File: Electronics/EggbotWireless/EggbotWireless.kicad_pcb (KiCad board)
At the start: 2 copper layers, 115 x 40 mm, 59 parts, among them J1 BATT, J2 Conn_01x04_Female, J3 USB_B_Micro, J4 AVR-ISP-6, J5 Conn_01x03_Female, M1 Stepper_Motor_bipolar, M2 Stepper_Motor_bipolar, M3 Motor_Servo, Q1 FDD8447L, Q2 2N7002, SW1 SW_SPDT, U1 TPS62203DBV, U2 ATmega32A-AU, U3 DW01, U4 FS8205A, U5 CP2102-GMR, U6 LTC4054ES5-4.2, U7 ESP-12E, U8 LM3478, Y1 16MHz

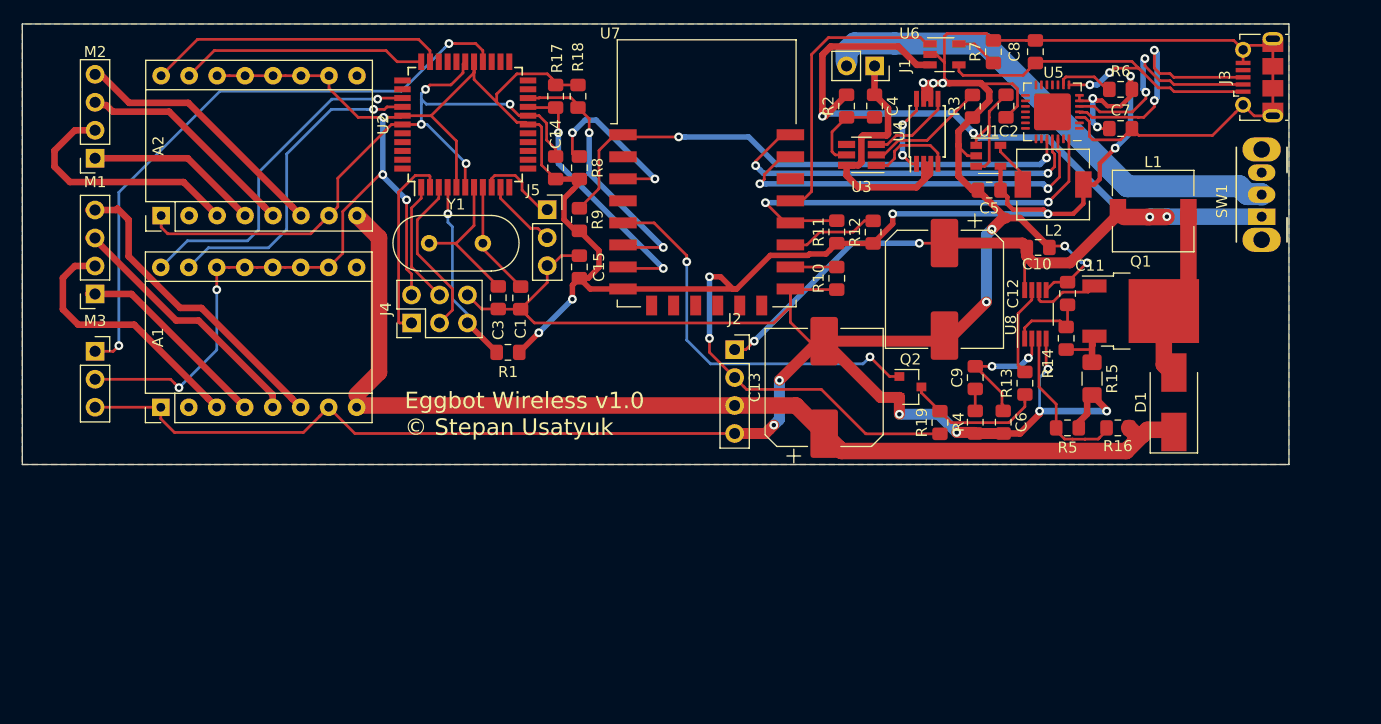
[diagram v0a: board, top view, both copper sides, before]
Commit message: use ft232rl for usb ic, better power handling
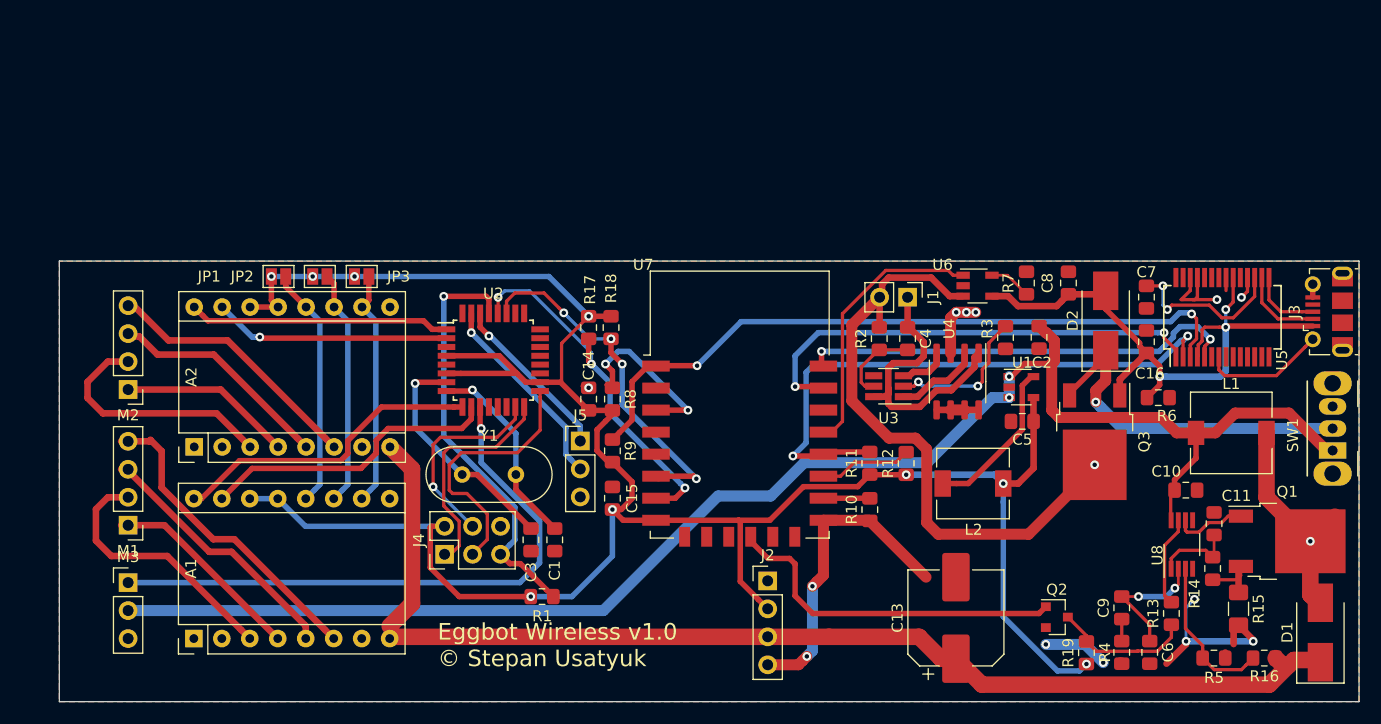
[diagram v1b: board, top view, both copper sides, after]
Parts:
- removed C12: 220uF, Capacitor_SMD:CP_Elec_10x10.5
- added C16: 100nf, Capacitor_SMD:C_0805_2012Metric_Pad1.15x1.40mm_HandSolder, F.Cu at (118.1, 44.9)
- added D2: SK84, Diode_SMD:D_SMB_Handsoldering, F.Cu at (114.4, 42.9)
- added JP1: , Jumper:SolderJumper-2_P1.3mm_Open_Pad1.0x1.5mm, F.Cu at (39.3, 38.9)
- added JP2: , Jumper:SolderJumper-2_P1.3mm_Open_Pad1.0x1.5mm, F.Cu at (43.0, 38.9)
- added JP3: , Jumper:SolderJumper-2_P1.3mm_Open_Pad1.0x1.5mm, F.Cu at (46.8, 38.9)
- added Q3: AOD403, Package_TO_SOT_SMD:TO-252-2, F.Cu at (113.4, 53.9)
- C13: footprint Capacitor_SMD:CP_Elec_10x10.5 -> Capacitor_SMD:CP_Elec_8x10.5
- J1: footprint Connector_PinSocket_2.54mm:PinSocket_1x02_P2.54mm_Vertical -> Connector_PinHeader_2.54mm:PinHeader_1x02_P2.54mm_Vertical
- J2: footprint Connector_PinSocket_2.54mm:PinSocket_1x04_P2.54mm_Vertical -> Connector_PinHeader_2.54mm:PinHeader_1x04_P2.54mm_Vertical
- J5, M3: footprint Connector_PinSocket_2.54mm:PinSocket_1x03_P2.54mm_Vertical -> Connector_PinHeader_2.54mm:PinHeader_1x03_P2.54mm_Vertical
- M1, M2: value Stepper_Motor_bipolar -> (none); footprint Connector_PinSocket_2.54mm:PinSocket_1x04_P2.54mm_Vertical -> Connector_PinHeader_2.54mm:PinHeader_1x04_P2.54mm_Vertical
- R7: value 1K6 -> 2.2K
- SW1: value SW_SPDT -> (none)
- U2: value ATmega32A-AU -> ATmega328P-AU; footprint Package_QFP:TQFP-44_10x10mm_P0.8mm -> Package_QFP:TQFP-32_7x7mm_P0.8mm
- U4: value FS8205A -> DMG4800LSD; footprint Package_SO:TSSOP-8_4.4x3mm_P0.65mm -> Package_SO:SO-8_3.9x4.9mm_P1.27mm
- U5: value CP2102-GMR -> FT232RL; footprint Package_DFN_QFN:QFN-28-1EP_5x5mm_P0.5mm_EP3.35x3.35mm -> Package_SO:SSOP-28_5.3x10.2mm_P0.65mm
- moved R6 28.2 mm to (119.1, 49.9), turned to 180 degrees
- moved L2 28.1 mm to (102.3, 57.7)
- moved C10 25.8 mm to (121.6, 58.3)
- moved D1 24.8 mm to (133.9, 71.2)
- moved R13 24.8 mm to (120.3, 69.5)
- moved C6 24.8 mm to (118.4, 73.1)
- moved Q1 24.8 mm to (130.8, 63.0)
- moved R15 24.8 mm to (126.4, 69.1)
- moved R4 24.8 mm to (115.8, 73.1)
- moved U8 24.8 mm to (121.3, 63.3)
- moved R19 24.8 mm to (112.6, 73.1)
- moved C11 24.8 mm to (124.2, 61.4)
- moved C9 24.8 mm to (115.8, 69.0)
- moved R14 24.8 mm to (124.1, 65.4)
- moved R5 24.8 mm to (124.2, 73.6)
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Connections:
- A1 pad 10: +3V3 -> Net-(A1-Pad10)
- A1 pad 11: +3V3 -> Net-(A1-Pad11)
- A1 pad 12: +3V3 -> Net-(A1-Pad12)
- A1 pad 15: Net-(A1-Pad15) -> STEP1
- A1 pad 16: Net-(A1-Pad16) -> DIR1
- A1 pad 2: Net-(A1-Pad2) -> (no net)
- A1 pad 9: Net-(A1-Pad9) -> (no net)
- A2 pad 10: +3V3 -> Net-(A1-Pad10)
- A2 pad 11: +3V3 -> Net-(A1-Pad11)
- A2 pad 12: +3V3 -> Net-(A1-Pad12)
- A2 pad 15: Net-(A2-Pad15) -> STEP2
- A2 pad 16: Net-(A2-Pad16) -> DIR2
- A2 pad 2: Net-(A2-Pad2) -> (no net)
- A2 pad 9: Net-(A2-Pad9) -> (no net)
- C10 pad 1: +BATT -> +5V
- C2 pad 1: +BATT -> +5V
- C7 pad 1: +3V3 -> GND
- C7 pad 2: GND -> Net-(C7-Pad2)
- J2 pad 1: +BATT -> (no net)
- J3 pad 2: Net-(J3-Pad2) -> USBD-
- J3 pad 3: Net-(J3-Pad3) -> USBD+
- J3 pad 4: Net-(J3-Pad4) -> (no net)
- L1 pad 1: +BATT -> +5V
- M3 pad 2: +3V3 -> +5V
- R1 pad 1: Net-(J4-Pad5) -> +3V3
- R1 pad 2: +3V3 -> Net-(J4-Pad5)
- R2 pad 2: +BATT -> Net-(J1-Pad2)
- R6 pad 1: Net-(R6-Pad1) -> GND
- R6 pad 2: +3V3 -> VBUS
- SW1 pad 1: +BATT -> +5V
- SW1 pad 2: Net-(J1-Pad2) -> Net-(D2-Pad1)
- SW1 pad 3: Net-(SW1-Pad3) -> (no net)
- U1 pad 1: +BATT -> +5V
- U1 pad 3: +BATT -> +5V
- U2 pad 1: Net-(J4-Pad4) -> DIR2
- U2 pad 10: Net-(J5-Pad2) -> STEP1
- U2 pad 11: Net-(U2-Pad11) -> Net-(M3-Pad1)
- U2 pad 12: Net-(U2-Pad12) -> (no net)
- U2 pad 13: Net-(U2-Pad13) -> (no net)
- U2 pad 14: Net-(U2-Pad14) -> (no net)
- U2 pad 15: Net-(U2-Pad15) -> Net-(J4-Pad4)
- U2 pad 16: Net-(U2-Pad16) -> Net-(J4-Pad1)
- U2 pad 17: +3V3 -> Net-(J4-Pad3)
- U2 pad 18: GND -> +3V3
- U2 pad 19: SCL -> (no net)
- U2 pad 2: Net-(J4-Pad1) -> STEP2
- U2 pad 20: SDA -> (no net)
- U2 pad 21: Net-(U2-Pad21) -> GND
- U2 pad 22: Net-(U2-Pad22) -> (no net)
- U2 pad 23: Net-(U2-Pad23) -> (no net)
- U2 pad 24: Net-(U2-Pad24) -> (no net)
- U2 pad 25: Net-(U2-Pad25) -> (no net)
- U2 pad 26: Net-(M3-Pad1) -> (no net)
- U2 pad 27: +3V3 -> SDA
- U2 pad 28: GND -> SCL
- U2 pad 29: Net-(U2-Pad29) -> Net-(J4-Pad5)
- U2 pad 3: Net-(J4-Pad3) -> GND
- U2 pad 30: Net-(U2-Pad30) -> Net-(J5-Pad1)
- U2 pad 31: Net-(U2-Pad31) -> Net-(J5-Pad2)
- U2 pad 32: Net-(A2-Pad16) -> (no net)
- U2 pad 4: Net-(J4-Pad5) -> +3V3
- U2 pad 5: +3V3 -> GND
- U2 pad 6: GND -> +3V3
- U2 pad 9: Net-(J5-Pad1) -> DIR1
- U3 pad 4: Net-(U3-Pad4) -> (no net)
- U4 pad 1: Net-(U4-Pad1) -> Net-(C4-Pad1)
- U4 pad 2: Net-(C4-Pad1) -> Net-(U3-Pad1)
- U4 pad 3: Net-(C4-Pad1) -> GND
- U4 pad 4: Net-(U3-Pad1) -> Net-(U3-Pad3)
- U4 pad 5: Net-(U3-Pad3) -> Net-(U4-Pad5)
- U4 pad 6: GND -> Net-(U4-Pad5)
- U4 pad 7: GND -> Net-(U4-Pad5)
- U4 pad 8: Net-(U4-Pad1) -> Net-(U4-Pad5)
- U5 pad 1: Net-(U5-Pad1) -> TXD_USB
- U5 pad 10: Net-(U5-Pad10) -> (no net)
- U5 pad 11: Net-(U5-Pad11) -> (no net)
- U5 pad 12: Net-(U5-Pad12) -> (no net)
- U5 pad 13: Net-(U5-Pad13) -> (no net)
- U5 pad 14: Net-(U5-Pad14) -> (no net)
- U5 pad 15: Net-(U5-Pad15) -> USBD+
- U5 pad 16: Net-(U5-Pad16) -> USBD-
- U5 pad 17: Net-(U5-Pad17) -> Net-(C7-Pad2)
- U5 pad 18: Net-(U5-Pad18) -> GND
- U5 pad 19: Net-(U5-Pad19) -> (no net)
- U5 pad 2: Net-(U5-Pad2) -> DTR_USB
- U5 pad 20: Net-(U5-Pad20) -> VBUS
- U5 pad 21: Net-(U5-Pad21) -> GND
- U5 pad 22: Net-(U5-Pad22) -> (no net)
- U5 pad 23: Net-(U5-Pad23) -> (no net)
- U5 pad 24: RTS_USB -> (no net)
- U5 pad 25: RXD_USB -> GND
- U5 pad 26: TXD_USB -> GND
- U5 pad 27: Net-(U5-Pad27) -> (no net)
- U5 pad 28: DTR_USB -> (no net)
- U5 pad 3: GND -> RTS_USB
- U5 pad 4: Net-(J3-Pad3) -> VBUS
- U5 pad 5: Net-(J3-Pad2) -> RXD_USB
- U5 pad 6: +3V3 -> (no net)
- U5 pad 7: +3V3 -> GND
- U5 pad 8: VBUS -> (no net)
- U5 pad 9: Net-(R6-Pad1) -> (no net)
- U6 pad 3: +BATT -> Net-(J1-Pad2)
- U7 pad 10: Net-(U7-Pad10) -> (no net)
- U7 pad 11: Net-(U7-Pad11) -> (no net)
- U7 pad 12: Net-(U7-Pad12) -> 12V_SWITCH
- U7 pad 13: Net-(U7-Pad13) -> (no net)
- U7 pad 14: Net-(U7-Pad14) -> (no net)
- U7 pad 2: Net-(U7-Pad2) -> (no net)
- U7 pad 20: Net-(U7-Pad20) -> (no net)
- U7 pad 4: Net-(U7-Pad4) -> (no net)
- U7 pad 5: 12V_SWITCH -> (no net)
- U7 pad 9: Net-(U7-Pad9) -> (no net)
- U8 pad 8: +BATT -> +5V
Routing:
- net GND: track 373.7 -> 83.4 mm, vias 18 -> 13
- net +5V: track 0.00 -> 140.0 mm, vias 0 -> 2
- net +BATT: track 124.5 -> 0.00 mm, vias 6 -> 0
- net +3V3: track 258.9 -> 206.3 mm, vias 15 -> 9
- net Net-(D2-Pad1): track 0.00 -> 33.0 mm, vias 0 -> 1
- net Net-(A1-Pad16): track 31.4 -> 0.00 mm, vias 1 -> 0
- net Net-(A1-Pad15): track 29.5 -> 0.00 mm, vias 1 -> 0
- net DIR1: track 0.00 -> 28.5 mm
- net STEP1: track 0.00 -> 27.4 mm
- net Net-(A2-Pad16): track 27.2 -> 0.00 mm
- net DIR2: track 0.00 -> 23.7 mm
- net Net-(J3-Pad3): track 22.8 -> 0.00 mm, vias 2 -> 0
- net Net-(J4-Pad5): track 16.0 -> 38.5 mm
- net Net-(A2-Pad15): track 22.4 -> 0.00 mm
- net Net-(A1-Pad12): track 0.00 -> 22.0 mm
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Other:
- board size 115 x 40 mm -> 118 x 40 mm
- net class Default: trace_width 0.25 -> 0.3
- rule trace_min: 0.2 -> 0.3

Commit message: add uart pin header for esp12
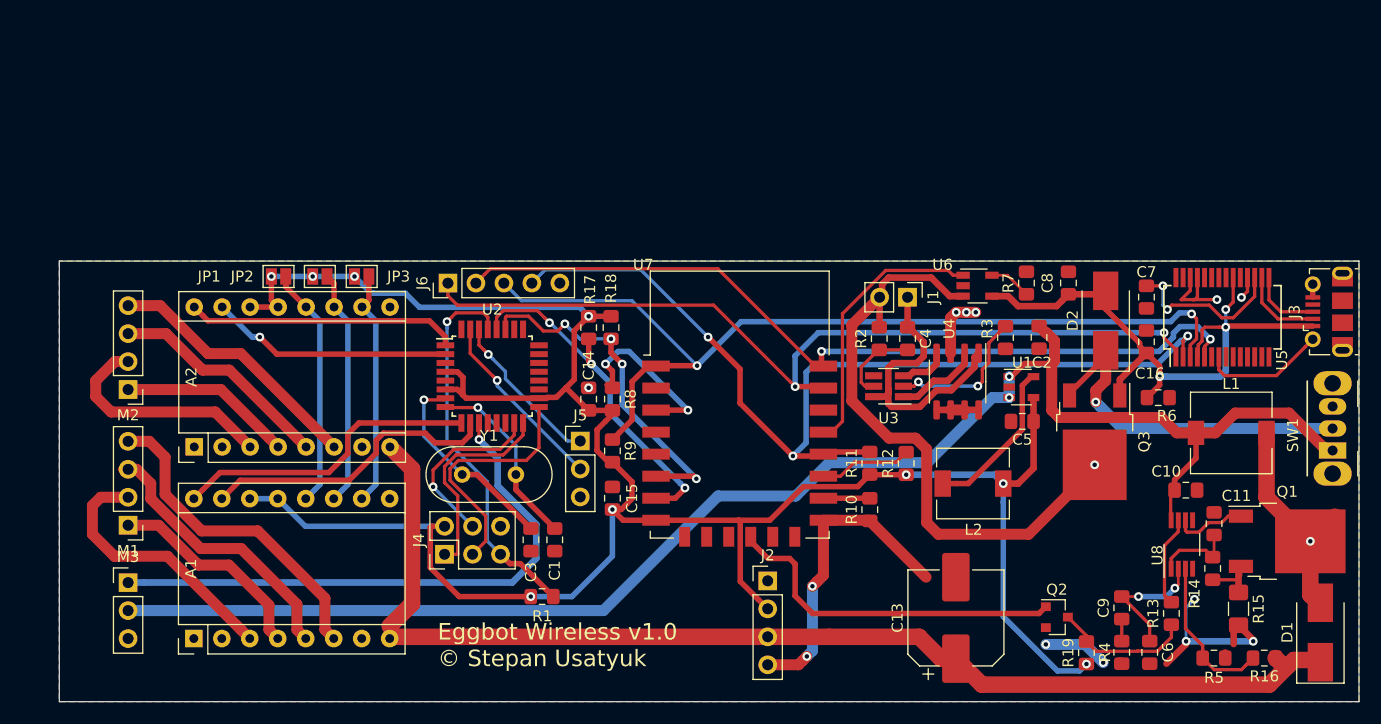
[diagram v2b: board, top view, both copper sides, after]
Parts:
- added J6: Conn_01x05_Male, Connector_PinHeader_2.54mm:PinHeader_1x05_P2.54mm_Vertical, F.Cu at (54.6, 39.5)
- moved U2 1.45 mm to (58.7, 48.0)
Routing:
- net TXD_USB: track 42.4 -> 78.5 mm
- net RXD_USB: track 40.9 -> 75.9 mm
- net DTR_USB: track 53.6 -> 86.6 mm, vias 2 -> 3
- net RTS_USB: track 64.0 -> 84.7 mm
- net Net-(J4-Pad5): track 38.5 -> 34.8 mm
- net +3V3: track 206.3 -> 203.2 mm
- net Net-(C3-Pad2): track 21.2 -> 18.5 mm
- net Net-(M3-Pad1): track 54.5 -> 52.4 mm
- net Net-(J4-Pad4): track 18.4 -> 16.4 mm
- net Net-(J4-Pad3): track 24.0 -> 22.2 mm
- net SCL: track 33.9 -> 32.4 mm
- net Net-(J5-Pad2): track 18.2 -> 16.8 mm
- net Net-(A1-Pad5): track 23.8 -> 25.2 mm
- net Net-(J4-Pad1): track 20.3 -> 19.1 mm
- net Net-(C1-Pad1): track 18.1 -> 16.8 mm
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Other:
- rule trace_min: 0.3 -> 0.2

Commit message: pcb v1.1 proto
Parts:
- added R20: 100K, Resistor_SMD:R_0805_2012Metric_Pad1.15x1.40mm_HandSolder, F.Cu at (110.0, 65.6)
- R6: value 10K -> 100K
- moved U8 0.66 mm to (120.6, 63.1)
- moved L2 0.30 mm to (102.6, 57.7)
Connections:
- U7 pad 12: 12V_SWITCH -> (no net)
- U7 pad 20: (no net) -> 12V_SWITCH
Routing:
- net 12V_SWITCH: track 31.9 -> 35.6 mm, vias 0 -> 2
- net GND: track 82.3 -> 79.2 mm, vias 13 -> 14
- net Net-(Q1-Pad1): track 6.63 -> 7.40 mm
- net Net-(J1-Pad2): track 56.5 -> 57.3 mm
- net Net-(R13-Pad2): track 8.21 -> 8.86 mm
- net Net-(C11-Pad2): track 7.33 -> 7.97 mm
- net RXD_USB: track 75.9 -> 76.5 mm
- net +3V3: track 203.2 -> 203.8 mm
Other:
- board text added: "Eggbot Wireless v1.1 © Stepan Usatyuk"
- board text removed: "Eggbot Wireless v1.0 © Stepan Usatyuk"

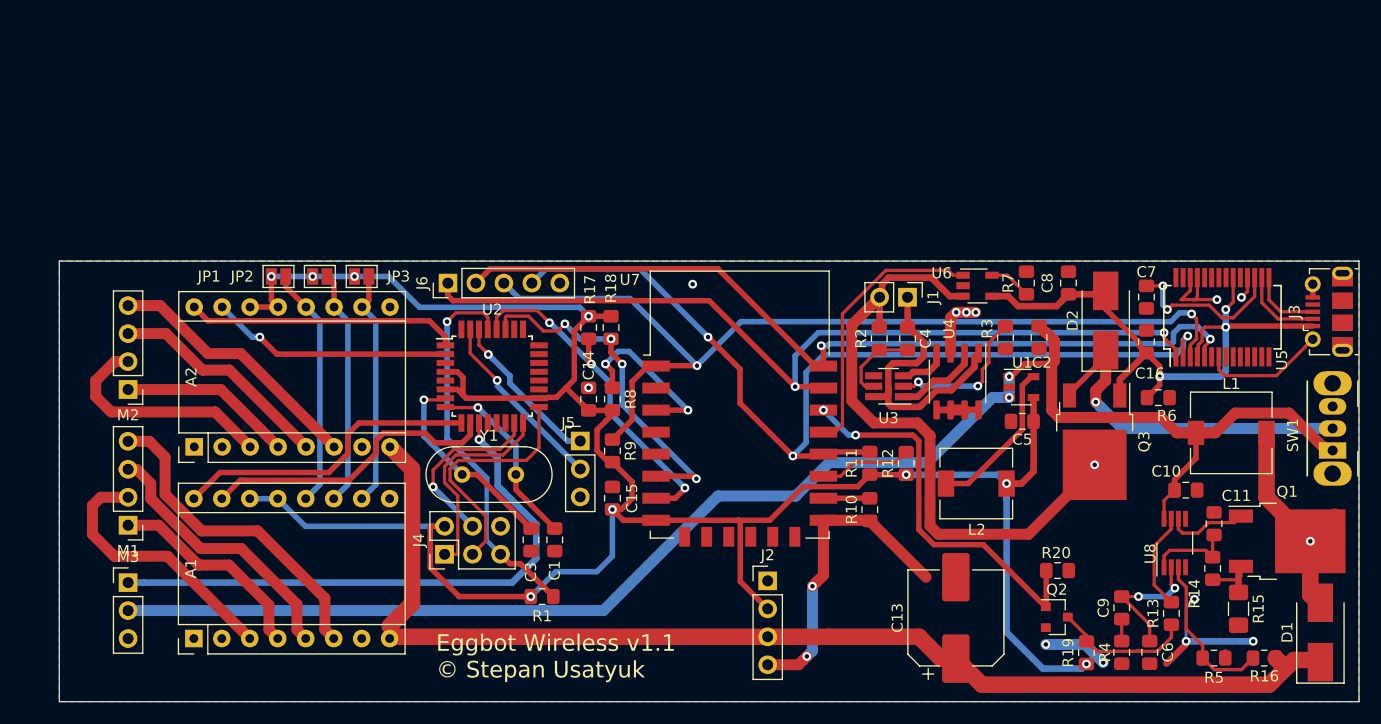
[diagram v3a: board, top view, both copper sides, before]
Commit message: use nodemcu reset circuit
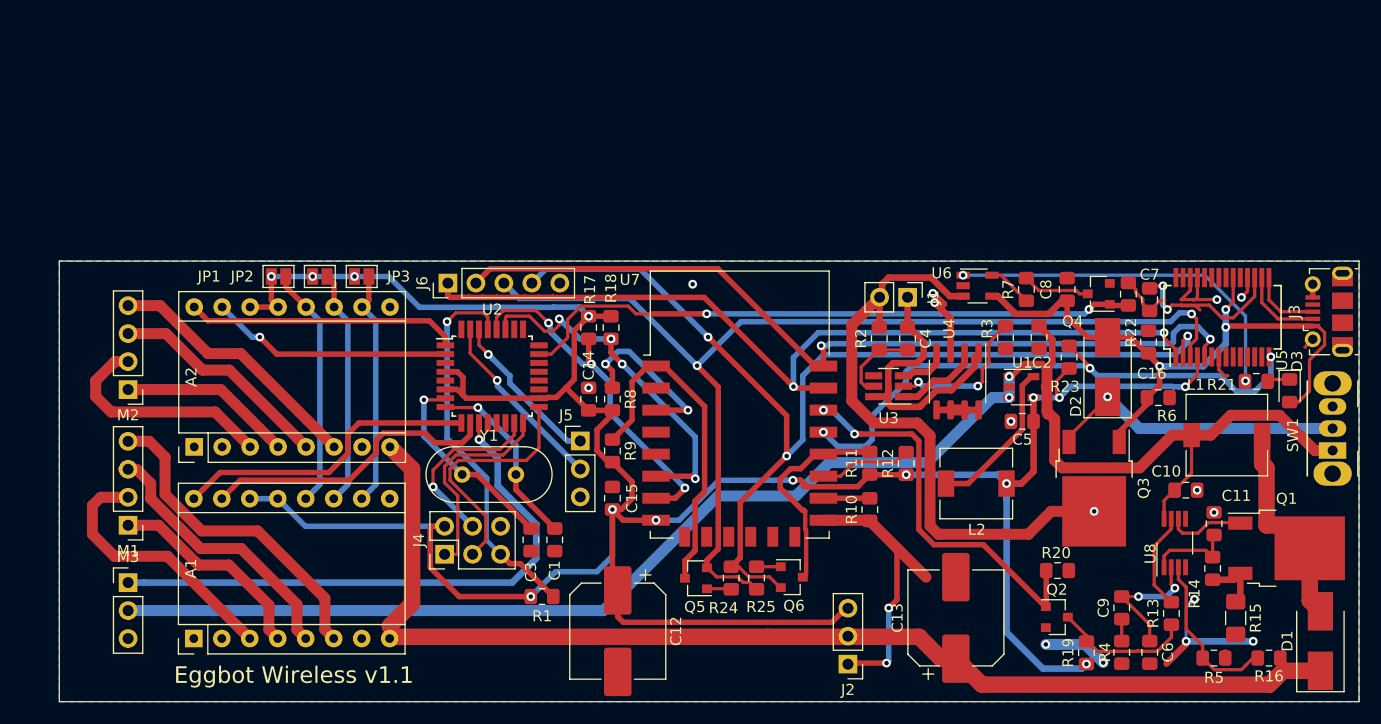
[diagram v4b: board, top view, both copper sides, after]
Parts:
- added C12: 220uF, Capacitor_SMD:CP_Elec_8x10.5, F.Cu at (70.1, 71.1)
- added D3: LED, Diode_SMD:D_0805_2012Metric_Pad1.15x1.40mm_HandSolder, F.Cu at (131.1, 49.3)
- added Q4: 2N7002, Package_TO_SOT_SMD:SOT-23, F.Cu at (113.7, 40.5)
- added Q5: S8050, Package_TO_SOT_SMD:SOT-23, F.Cu at (77.2, 66.3)
- added Q6: S8050, Package_TO_SOT_SMD:SOT-23, F.Cu at (85.9, 66.2)
- added R21: 330, Resistor_SMD:R_0805_2012Metric_Pad1.15x1.40mm_HandSolder, F.Cu at (128.0, 48.5)
- added R22: 100K, Resistor_SMD:R_0805_2012Metric_Pad1.15x1.40mm_HandSolder, F.Cu at (116.4, 40.5)
- added R23: 10K, Resistor_SMD:R_0805_2012Metric_Pad1.15x1.40mm_HandSolder, F.Cu at (111.0, 46.3)
- added R24: 12K, Resistor_SMD:R_0805_2012Metric_Pad1.15x1.40mm_HandSolder, F.Cu at (80.4, 66.3)
- added R25: 12K, Resistor_SMD:R_0805_2012Metric_Pad1.15x1.40mm_HandSolder, F.Cu at (82.7, 66.3)
- J2: value Conn_01x04_Female -> Conn_01x03_Male; footprint Connector_PinHeader_2.54mm:PinHeader_1x04_P2.54mm_Vertical -> Connector_PinHeader_2.54mm:PinHeader_1x03_P2.54mm_Vertical
- moved J2 10.5 mm to (91.0, 74.1), turned to 180 degrees
- moved D2 4.23 mm to (114.5, 47.2)
- moved Q3 4.23 mm to (113.3, 58.2)
- moved R15 0.88 mm to (126.2, 69.9)
- moved D1 0.78 mm to (133.9, 72.0)
- moved Q1 0.64 mm to (130.8, 63.6)
- moved C8 0.59 mm to (110.9, 40.1)
- moved R7 0.58 mm to (107.2, 40.1)
- moved L1 0.45 mm to (125.4, 53.3)
- moved R16 0.42 mm to (129.2, 73.6)
- moved C7 0.37 mm to (118.4, 41.0)
- moved C16 0.19 mm to (118.3, 44.9)
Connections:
- J2 pad 1: (no net) -> GND
- J2 pad 2: +3V3 -> +12V
- J2 pad 3: +12V -> +3V3
- R11 pad 2: DTR_USB -> GPIO0
- R7 pad 2: GND -> Net-(Q4-Pad3)
- R9 pad 1: RTS_USB -> ESPRST
- U2 pad 23: (no net) -> CHEN
- U5 pad 14: (no net) -> PWREN
- U5 pad 4: VBUS -> +3V3
- U7 pad 1: RTS_USB -> ESPRST
- U7 pad 18: DTR_USB -> GPIO0
- U7 pad 19: CHRG -> PWREN
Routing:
- net CHEN: track 0.00 -> 57.0 mm, vias 0 -> 2
- net PWREN: track 0.00 -> 52.2 mm, vias 0 -> 3
- net +3V3: track 203.8 -> 247.6 mm, vias 9 -> 14
- net ESPRST: track 0.00 -> 31.4 mm
- net GPIO0: track 0.00 -> 19.8 mm
- net RTS_USB: track 84.7 -> 96.7 mm
- net DTR_USB: track 87.1 -> 97.0 mm
- net CHRG: track 24.9 -> 33.1 mm, vias 0 -> 2
- net Net-(Q4-Pad3): track 0.00 -> 6.46 mm
- net Net-(D2-Pad1): track 33.0 -> 27.2 mm
- net +5V: track 140.1 -> 144.9 mm
- net GND: track 79.2 -> 74.9 mm, vias 14 -> 16
- net Net-(Q5-Pad1): track 0.00 -> 2.22 mm
- net Net-(Q6-Pad1): track 0.00 -> 2.20 mm
- net Net-(D3-Pad1): track 0.00 -> 2.07 mm
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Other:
- board text added: "Eggbot Wireless v1.1"
- board text removed: "Eggbot Wireless v1.1 © Stepan Usatyuk"
